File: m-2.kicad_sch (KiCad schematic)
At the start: 56 parts, among them J1 2199230-6, J2 1-2199230-6, M2 M2_4222, M3 M2_2280, U2 74LVC2G07GV, U3 74LVC2G07GV, Y1 ECS-327MVATX-2-CN-TR3

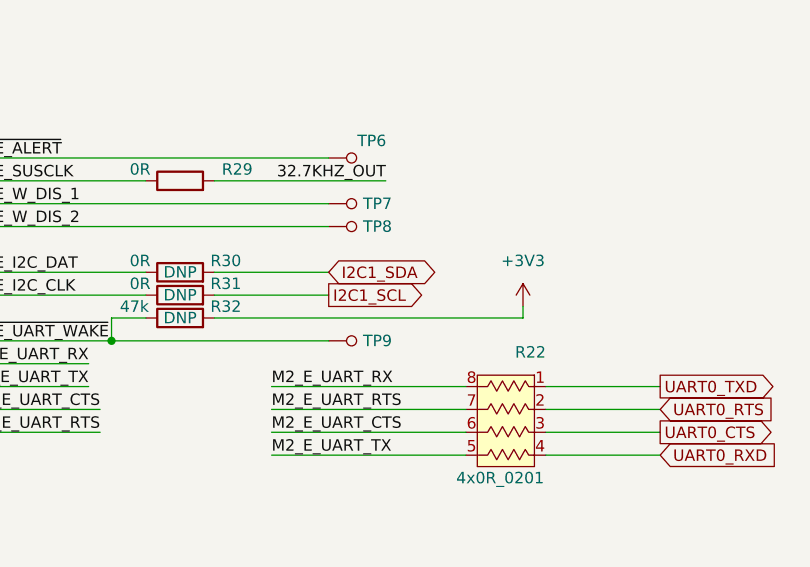
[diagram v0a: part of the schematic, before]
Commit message: Routed all traces
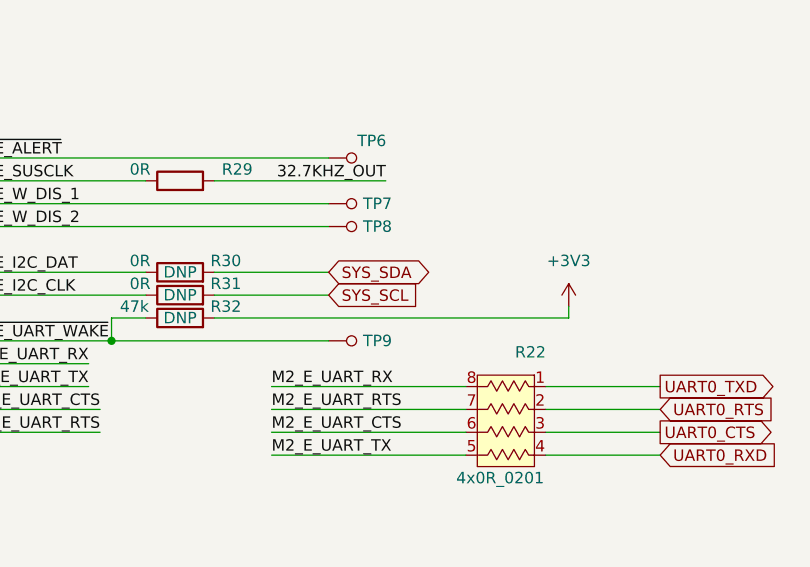
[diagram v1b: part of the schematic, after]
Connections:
- net I2C1_SCL renamed SYS_SCL
- net I2C1_SDA renamed SYS_SDA
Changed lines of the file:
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@@
     (stroke (width 0) (type default) (color 0 0 0 0))
   )
-  (wire (pts (xy 293.37 177.8) (xy 293.37 179.07))
+  (wire (pts (xy 298.45 177.8) (xy 298.45 179.07))
     (stroke (width 0) (type default) (color 0 0 0 0))
   )
@@
     (stroke (width 0) (type default) (color 0 0 0 0))
   )
-  (wire (pts (xy 259.08 179.07) (xy 293.37 179.07))
+  (wire (pts (xy 259.08 179.07) (xy 298.45 179.07))
     (stroke (width 0) (type default) (color 0 0 0 0))
   )
@@
     )
   )
-  (global_label "I2C1_SDA" (shape bidirectional) (at 271.78 173.99 0)
-    (effects (font (size 1.27 1.27)) (justify left))
-    (property "Intersheet References" "${INTERSHEET_REFS}" (id 0) (at 284.48 173.99 0)
-      (effects (font (size 1.27 1.27)) (justify left))
-    )
-  )
   (global_label "PCIE0_RX2_P" (shape output) (at 267.97 95.25 180)
     (effects (font (size 1.27 1.27)) (justify right))
@@
     )
   )
-  (global_label "I2C1_SCL" (shape output) (at 271.78 176.53 0)
-    (effects (font (size 1.27 1.27)) (justify left))
-    (property "Intersheet References" "${INTERSHEET_REFS}" (id 0) (at 284.48 176.53 0)
-      (effects (font (size 1.27 1.27)) (justify left))
-    )
-  )
   (global_label "PCIE0_TX1_N" (shape input) (at 267.97 74.93 180)
     (effects (font (size 1.27 1.27)) (justify right))
@@
     )
   )
+  (global_label "SYS_SCL" (shape input) (at 271.78 176.53 0)
+    (effects (font (size 1.27 1.27)) (justify left))
+    (property "Intersheet References" "${INTERSHEET_REFS}" (id 0) (at 284.48 176.53 0)
+      (effects (font (size 1.27 1.27)) (justify left))
+    )
+  )
   (global_label "PCIE1_CLK_N" (shape input) (at 151.13 173.99 180)
     (effects (font (size 1.27 1.27)) (justify right))
@@
     )
   )
+  (global_label "SYS_SDA" (shape bidirectional) (at 271.78 173.99 0)
+    (effects (font (size 1.27 1.27)) (justify left))
+    (property "Intersheet References" "${INTERSHEET_REFS}" (id 0) (at 284.48 173.99 0)
+      (effects (font (size 1.27 1.27)) (justify left))
+    )
+  )
   (global_label "I2S1_LRCK" (shape output) (at 156.21 229.87 180)
     (effects (font (size 1.27 1.27)) (justify right))
@@
     (pin "2")
   )
-  (symbol (lib_id "power:+3V3") (at 293.37 177.8 0) (unit 1)
+  (symbol (lib_id "power:+3V3") (at 298.45 177.8 0) (unit 1)
     (in_bom yes) (on_board yes) (fields_autoplaced)
-    (property "Reference" "#PWR033" (id 0) (at 293.37 181.61 0)
+    (property "Reference" "#PWR033" (id 0) (at 298.45 181.61 0)
       (effects (font (size 1.27 1.27)) hide)
     )
-    (property "Value" "+3V3" (id 1) (at 293.37 172.72 0))
-    (property "Footprint" "" (id 2) (at 293.37 177.8 0)
+    (property "Value" "+3V3" (id 1) (at 298.45 172.72 0))
+    (property "Footprint" "" (id 2) (at 298.45 177.8 0)
       (effects (font (size 1.27 1.27)) hide)
     )
-    (property "Datasheet" "" (id 3) (at 293.37 177.8 0)
+    (property "Datasheet" "" (id 3) (at 298.45 177.8 0)
       (effects (font (size 1.27 1.27)) hide)
     )

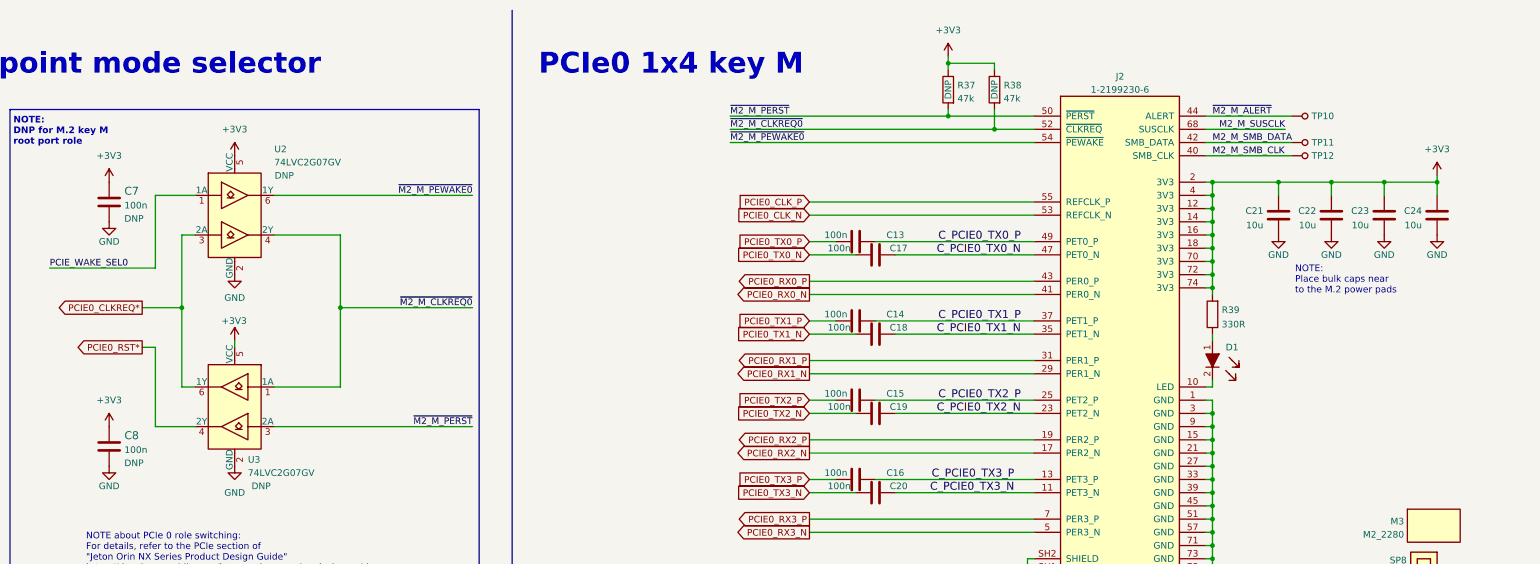
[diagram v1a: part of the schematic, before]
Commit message: Manufacturability improvements and PCIe length matching
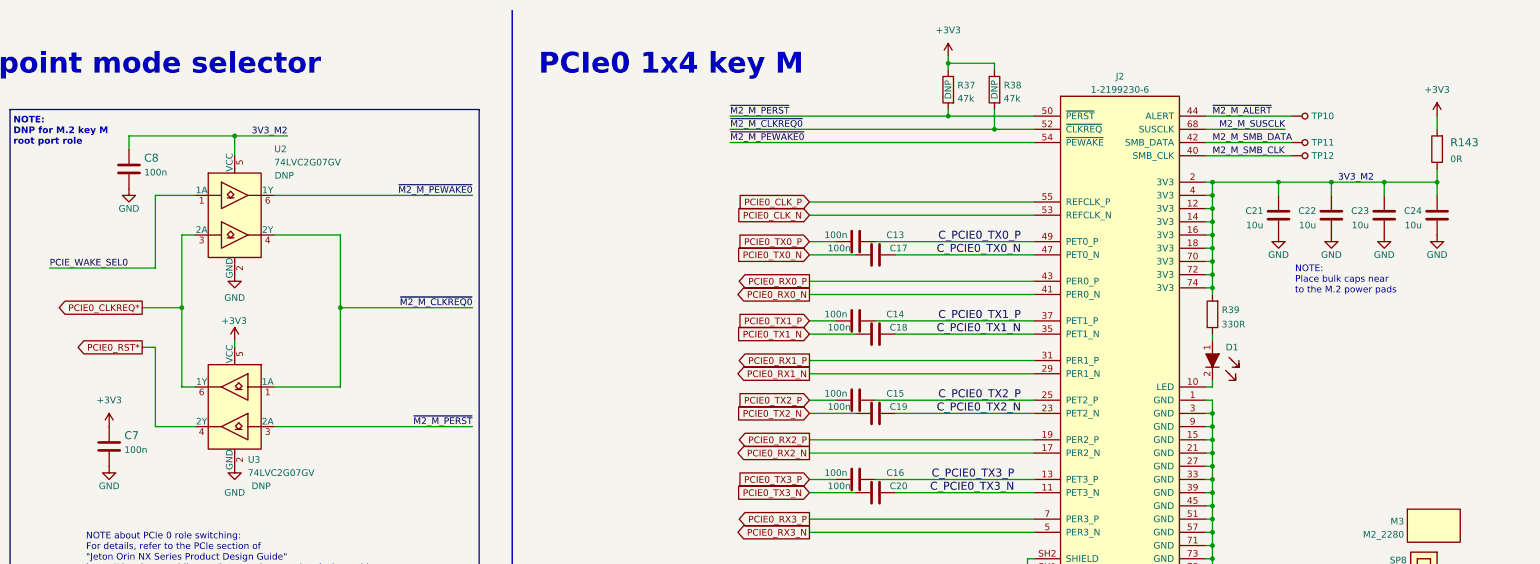
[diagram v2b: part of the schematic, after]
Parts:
- added R143: R_0R_0805, antmicro-footprints:0805-res, symbol antmicroResistorsmisc:R_0R_0805
- C7, C8: DNP DNP -> (none)
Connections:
- net +3V3: now also R143.2; no longer C21.1, C22.1, C23.1, C24.1, C8.1, J2.12 (3V3), J2.14 (3V3), J2.16 (3V3), J2.18 (3V3), J2.2 (3V3), J2.4 (3V3), J2.70 (3V3), J2.72 (3V3), J2.74 (3V3), R39.2, U2.5 (VCC)
- new net 3V3_M2: C21.1, C22.1, C23.1, C24.1, C8.1, J2.12 (3V3), J2.14 (3V3), J2.16 (3V3), J2.18 (3V3), J2.2 (3V3), J2.4 (3V3), J2.70 (3V3), J2.72 (3V3), J2.74 (3V3), R143.1, R39.2, U2.5 (VCC)
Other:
- moved on the sheet: C7, C8

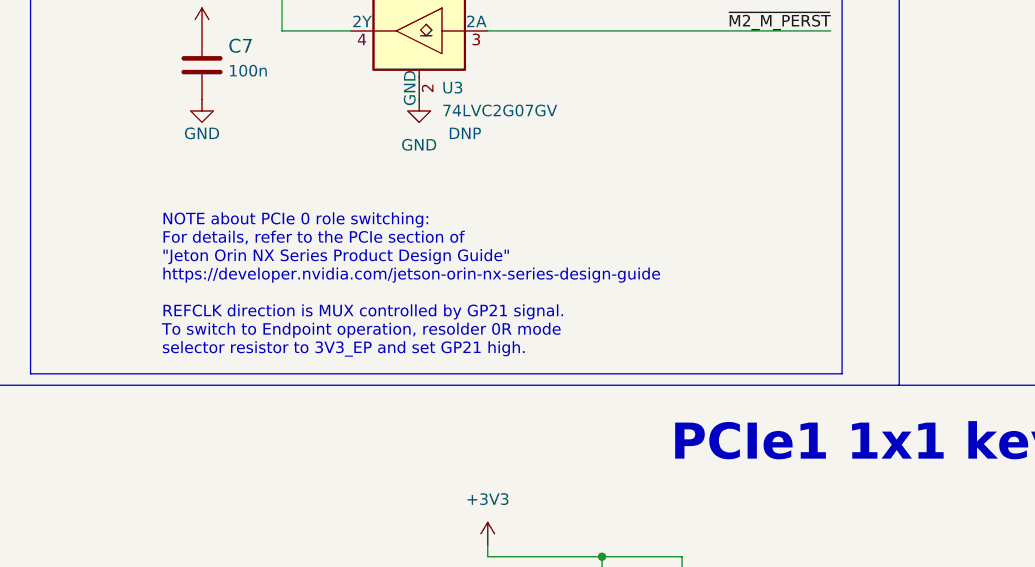
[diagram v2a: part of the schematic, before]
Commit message: M.2 SCH: Remove obsolete note about PCIe0 Root Port / Endpoint switching
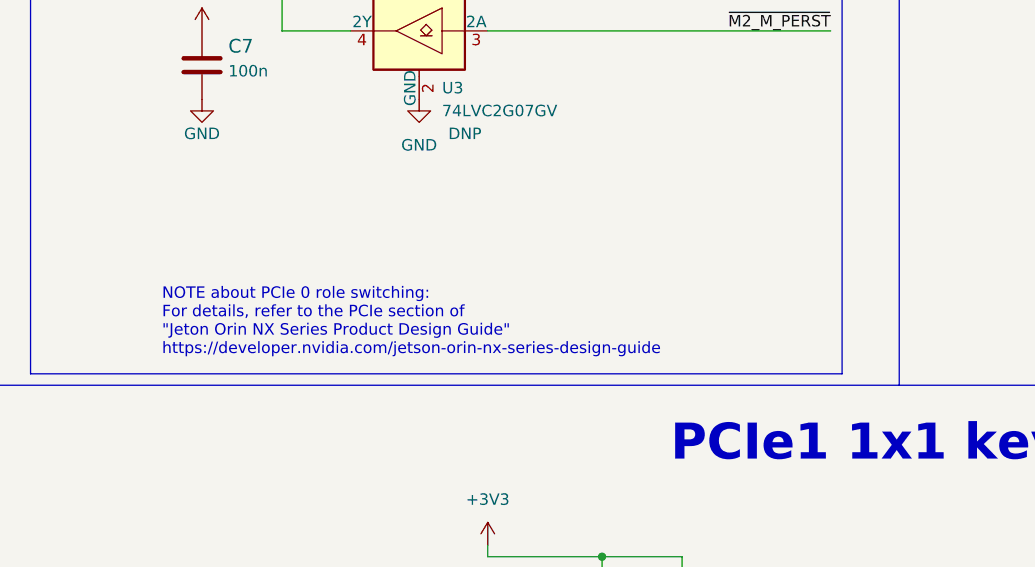
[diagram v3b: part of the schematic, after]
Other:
- note added: "NOTE about PCIe 0 role switching: For details, refer to the PCIe section of "Jeton Orin NX Series Product Design Guide" https://developer.nvidia.com/jetson-orin-nx-series-design-guide"
- note removed: "NOTE about PCIe 0 role switching: For details, refer to the PCIe section of "Jeton Orin NX Series Product Design Guide" https://developer.nvidia.com/jetson-orin-nx-series-design-guide REFCLK direction is MUX controlled by GP21 signal. To switch to Endpoint operation, resolder 0R mode selector resistor to 3V3_EP and set GP21 high."
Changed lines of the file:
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@@
     (effects (font (size 4 4) (thickness 0.8) bold) (justify left bottom))
   )
-  (text "NOTE about PCIe 0 role switching:\nFor details, refer to the PCIe section of \n\"Jeton Orin NX Series Product Design Guide\"\nhttps://developer.nvidia.com/jetson-orin-nx-series-design-guide\n\nREFCLK direction is MUX controlled by GP21 signal.\nTo switch to Endpoint operation, resolder 0R mode\nselector resistor to 3V3_EP and set GP21 high."
+  (text "NOTE about PCIe 0 role switching:\nFor details, refer to the PCIe section of \n\"Jeton Orin NX Series Product Design Guide\"\nhttps://developer.nvidia.com/jetson-orin-nx-series-design-guide"
     (at 128.905 128.905 0)
     (effects (font (size 1.27 1.27)) (justify left bottom))

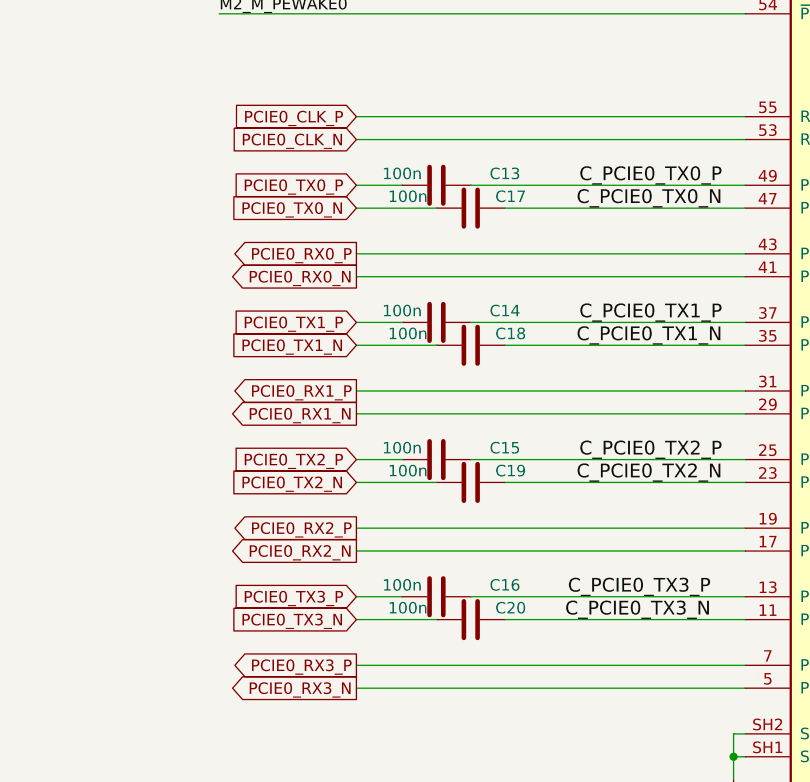
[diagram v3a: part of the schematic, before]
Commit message: CSchematic changes after review
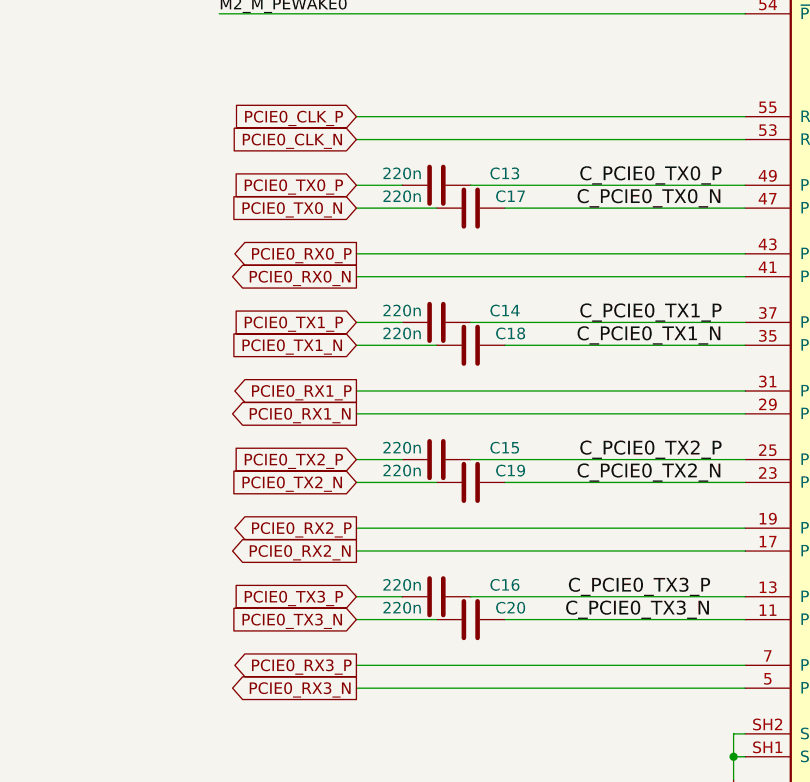
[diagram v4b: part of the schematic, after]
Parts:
- C13, C17: symbol antmicroCapacitors0402:C_100n_0402 -> antmicroCapacitors0402:C_220n_0402; MPN GRM155R61H104KE14D -> CC0402KRX5R6BB224; Manufacturer Murata -> Yaego; Val 100n -> 220n
- C14, C15, C16, C18, C19, C20: value C_100n_0402 -> C_220n_0402; symbol antmicroCapacitors0402:C_100n_0402 -> antmicroCapacitors0402:C_220n_0402; MPN GRM155R61H104KE14D -> CC0402KRX5R6BB224; Manufacturer Murata -> Yaego; Val 100n -> 220n

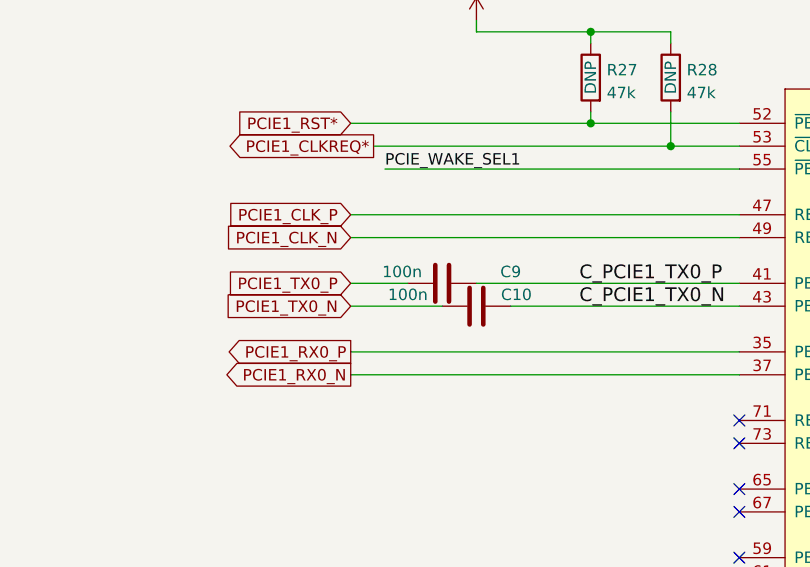
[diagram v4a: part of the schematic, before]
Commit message: Replace Key E PCIe capacitors with 220n ones
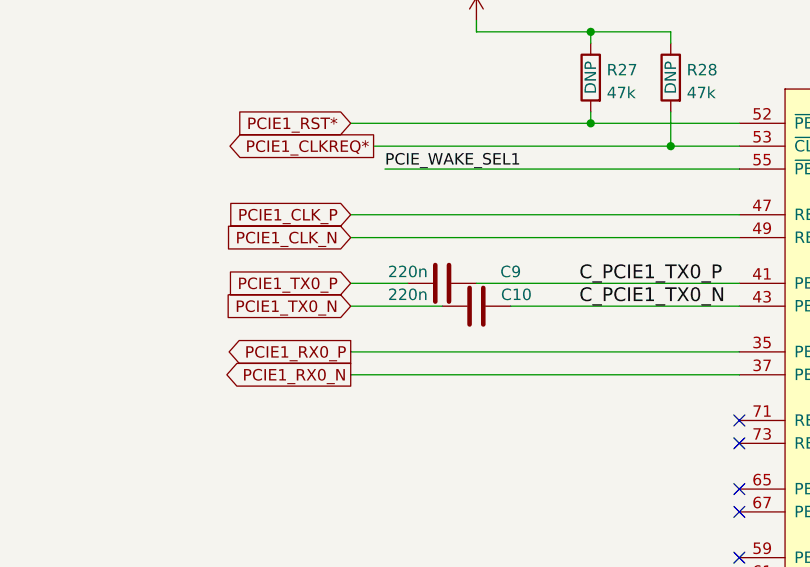
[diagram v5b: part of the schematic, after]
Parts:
- removed C10, C9: C_100n_0402, antmicro-footprints:0402-cap, symbol antmicroCapacitors0402:C_100n_0402
- added C10, C9: C_100n_0402, antmicro-footprints:0402-cap, symbol antmicroCapacitors0402:C_220n_0402
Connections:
- net C_PCIE1_TX0_N: now also C10.2
- net C_PCIE1_TX0_P: now also C9.2
- net PCIE1_TX0_N: now also C10.1
- net PCIE1_TX0_P: now also C9.1
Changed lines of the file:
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@@
     (pin "1")
-  )
-  (symbol (lib_id "antmicroCapacitors0402:C_100n_0402") (at 165.1 181.61 90) (unit 1)
-    (in_bom yes) (on_board yes)
-    (property "Reference" "C10" (id 0) (at 169.545 180.34 90))
-    (property "Value" "C_100n_0402" (id 1) (at 168.91 181.61 0)
-      (effects (font (size 1.27 1.27)) hide)
-    )
-    (property "Footprint" "antmicro-footprints:0402-cap" (id 2) (at 160.02 176.53 0)
-      (effects (font (size 1.524 1.524)) (justify left) hide)
-    )
-    (property "Datasheet" "" (id 3) (at 165.1 181.61 0)
-      (effects (font (size 1.27 1.27)) hide)
-    )
-    (property "Manufacturer" "Murata" (id 4) (at 154.94 176.53 0)
-      (effects (font (size 1.524 1.524)) (justify left) hide)
-    )
-    (property "MPN" "GRM155R61H104KE14D" (id 5) (at 157.48 176.53 0)
-      (effects (font (size 1.524 1.524)) (justify left) hide)
-    )
-    (property "Val" "100n" (id 6) (at 157.48 180.34 90))
-    (pin "1")
-    (pin "2")
   )
   (symbol (lib_id "antmicroResistors0402:R_0R_0402") (at 66.04 104.14 0) (unit 1)
@@
     )
     (pin "1")
-  )
-  (symbol (lib_id "antmicroCapacitors0402:C_100n_0402") (at 161.29 179.07 90) (unit 1)
-    (in_bom yes) (on_board yes)
-    (property "Reference" "C9" (id 0) (at 168.91 177.8 90))
-    (property "Value" "C_100n_0402" (id 1) (at 165.1 179.07 0)
-      (effects (font (size 1.27 1.27)) hide)
-    )
-    (property "Footprint" "antmicro-footprints:0402-cap" (id 2) (at 156.21 173.99 0)
-      (effects (font (size 1.524 1.524)) (justify left) hide)
-    )
-    (property "Datasheet" "" (id 3) (at 161.29 179.07 0)
-      (effects (font (size 1.27 1.27)) hide)
-    )
-    (property "Manufacturer" "Murata" (id 4) (at 151.13 173.99 0)
-      (effects (font (size 1.524 1.524)) (justify left) hide)
-    )
-    (property "MPN" "GRM155R61H104KE14D" (id 5) (at 153.67 173.99 0)
-      (effects (font (size 1.524 1.524)) (justify left) hide)
-    )
-    (property "Val" "100n" (id 6) (at 156.845 177.8 90))
-    (pin "1")
-    (pin "2")
   )
   (symbol (lib_id "antmicroResistors0402:R_47k_0402") (at 255.27 179.07 0) (unit 1)
@@
     )
   )
+  (symbol (lib_id "antmicroCapacitors0402:C_220n_0402") (at 165.1 181.61 90) (unit 1)
+    (in_bom yes) (on_board yes)
+    (property "Reference" "C10" (id 0) (at 169.545 180.34 90))
+    (property "Value" "C_100n_0402" (id 1) (at 168.91 181.61 0)
+      (effects (font (size 1.27 1.27)) hide)
+    )
+    (property "Footprint" "antmicro-footprints:0402-cap" (id 2) (at 160.02 176.53 0)
+      (effects (font (size 1.524 1.524)) (justify left) hide)
+    )
+    (property "Datasheet" "" (id 3) (at 165.1 181.61 0)
+      (effects (font (size 1.27 1.27)) hide)
+    )
+    (property "Manufacturer" "Yaego" (id 4) (at 154.94 176.53 0)
+      (effects (font (size 1.524 1.524)) (justify left) hide)
+    )
+    (property "MPN" "CC0402KRX5R6BB224" (id 5) (at 157.48 176.53 0)
+      (effects (font (size 1.524 1.524)) (justify left) hide)
+    )
+    (property "Val" "220n" (id 6) (at 157.48 180.34 90))
+    (pin "1")
+    (pin "2")
+  )
   (symbol (lib_id "antmicroCapacitors0402:C_220n_0402") (at 276.86 102.87 90) (unit 1)
     (in_bom yes) (on_board yes)
@@
     (pin "1")
     (pin "2")
+  )
+  (symbol (lib_id "antmicroCapacitors0402:C_220n_0402") (at 161.29 179.07 90) (unit 1)
+    (in_bom yes) (on_board yes)
+    (property "Reference" "C9" (id 0) (at 168.91 177.8 90))
+    (property "Value" "C_100n_0402" (id 1) (at 165.1 179.07 0)
+      (effects (font (size 1.27 1.27)) hide)
+    )
+    (property "Footprint" "antmicro-footprints:0402-cap" (id 2) (at 156.21 173.99 0)
+      (effects (font (size 1.524 1.524)) (justify left) hide)
+    )
+    (property "Datasheet" "" (id 3) (at 161.29 179.07 0)
+      (effects (font (size 1.27 1.27)) hide)
+    )
+    (property "Manufacturer" "Yaego" (id 4) (at 151.13 173.99 0)
+      (effects (font (size 1.524 1.524)) (justify left) hide)
+    )
+    (property "MPN" "CC0402KRX5R6BB224" (id 5) (at 153.67 173.99 0)
+      (effects (font (size 1.524 1.524)) (justify left) hide)
+    )
+    (property "Val" "220n" (id 6) (at 157.48 177.8 90))
+    (pin "1")
+    (pin "2")
